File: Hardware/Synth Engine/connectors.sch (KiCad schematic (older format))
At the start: 5 parts

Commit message: connect control board to main synth schem pages
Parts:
- removed J? (x4): Conn_01x12, symbol Conn_01x12
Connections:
- net labels added: freq_fb_1, freq_fb_2, freq_fb_3, freq_fb_4
- wire segments 97 -> 105
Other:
- moved on the sheet: J?

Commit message: remove extraneous net labels
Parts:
- removed J?: Conn_01x02, symbol Conn_01x02
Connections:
- net labels removed: LFO_freq_in, LFO_freq_out
- wire segments 105 -> 101
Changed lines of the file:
@@
 Text Label 1600 6250 0    60   ~ 0
 freq_out_4
-Text Label 8000 5750 2    60   ~ 0
-LFO_freq_in
-Text Label 8000 5850 2    60   ~ 0
-LFO_freq_out
 $Comp
 L +5V #PWR?
@@
 Wire Wire Line
 	1550 2050 1600 2050
-$Comp
-L Conn_01x02 J?
-U 1 1 5C5CD696
-P 4250 5000
-F 0 "J?" H 4250 5100 50  0000 C CNN
-F 1 "Conn_01x02" H 4250 4800 50  0000 C CNN
-F 2 "" H 4250 5000 50  0001 C CNN
-F 3 "" H 4250 5000 50  0001 C CNN
-	1    4250 5000
-	-1   0    0    -1
-$EndComp
-Wire Wire Line
-	4450 5000 4600 5000
-Wire Wire Line
-	4600 5100 4450 5100
 Wire Wire Line
 	1400 2450 1600 2450
@@
 Wire Wire Line
 	8000 5350 8300 5350
-Text HLabel 8300 5750 2    60   Input ~ 0
-LFO_freq_in
-Text HLabel 8300 5850 2    60   Output ~ 0
-LFO_freq_out
-Wire Wire Line
-	8300 5750 8000 5750
-Wire Wire Line
-	8000 5850 8300 5850
-Text Label 4600 5000 0    60   ~ 0
-LFO_freq_in
-Text Label 4600 5100 0    60   ~ 0
-LFO_freq_out
 Text Label 1600 1300 0    60   ~ 0
 freq_fb_1

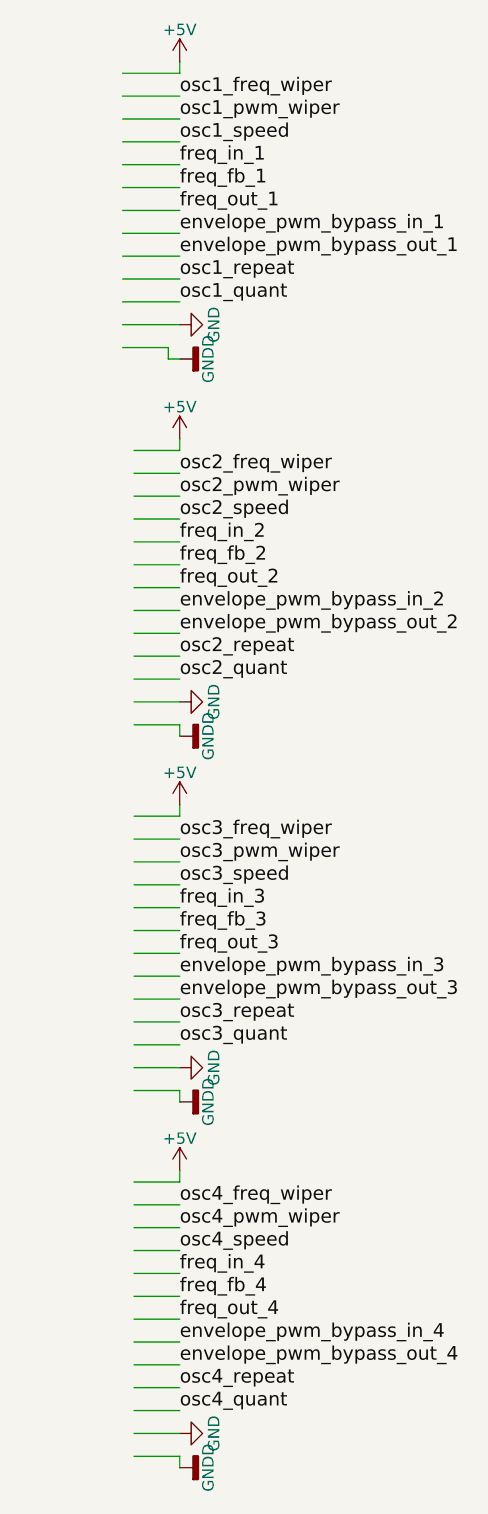
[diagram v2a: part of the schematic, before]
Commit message: fix missing connectors in main synth project
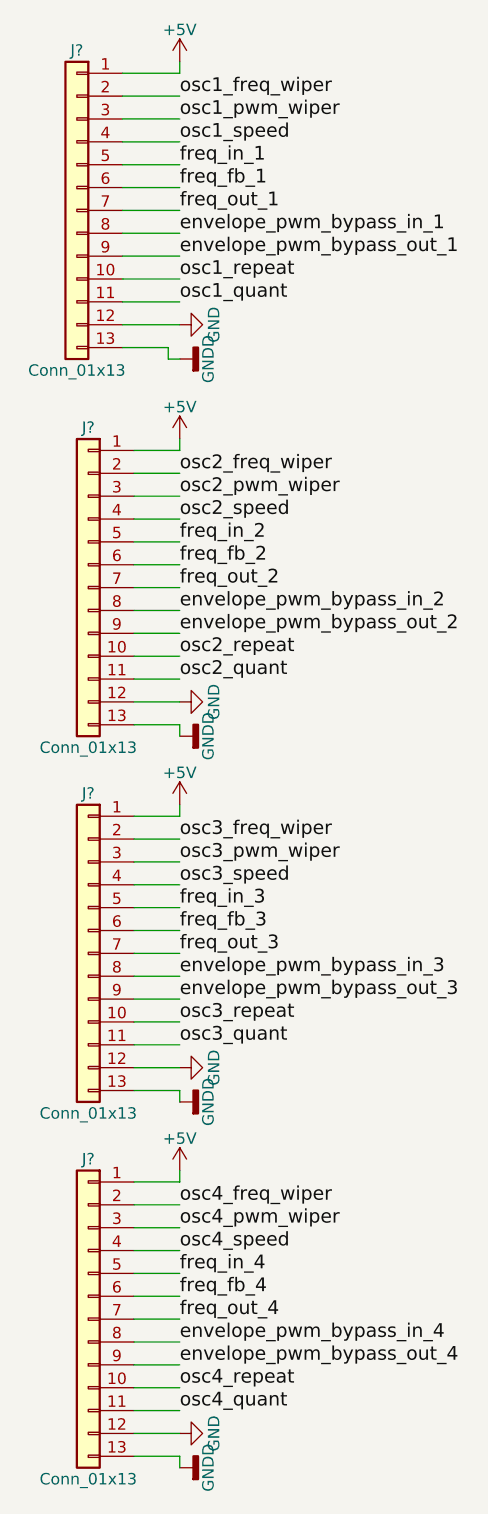
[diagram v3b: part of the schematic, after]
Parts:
- added J? (x4): Conn_01x13, symbol Conn_01x13
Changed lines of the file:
@@
 Wire Wire Line
 	8300 4850 8000 4850
+$Comp
+L Conn_01x13 J?
+U 1 1 5C5E7989
+P 1150 1400
+F 0 "J?" H 1150 2100 50  0000 C CNN
+F 1 "Conn_01x13" H 1150 700 50  0000 C CNN
+F 2 "" H 1150 1400 50  0001 C CNN
+F 3 "" H 1150 1400 50  0001 C CNN
+	1    1150 1400
+	-1   0    0    -1
+$EndComp
+$Comp
+L Conn_01x13 J?
+U 1 1 5C5E7A2D
+P 1200 3050
+F 0 "J?" H 1200 3750 50  0000 C CNN
+F 1 "Conn_01x13" H 1200 2350 50  0000 C CNN
+F 2 "" H 1200 3050 50  0001 C CNN
+F 3 "" H 1200 3050 50  0001 C CNN
+	1    1200 3050
+	-1   0    0    -1
+$EndComp
+$Comp
+L Conn_01x13 J?
+U 1 1 5C5E7A85
+P 1200 4650
+F 0 "J?" H 1200 5350 50  0000 C CNN
+F 1 "Conn_01x13" H 1200 3950 50  0000 C CNN
+F 2 "" H 1200 4650 50  0001 C CNN
+F 3 "" H 1200 4650 50  0001 C CNN
+	1    1200 4650
+	-1   0    0    -1
+$EndComp
+$Comp
+L Conn_01x13 J?
+U 1 1 5C5E7AE0
+P 1200 6250
+F 0 "J?" H 1200 6950 50  0000 C CNN
+F 1 "Conn_01x13" H 1200 5550 50  0000 C CNN
+F 2 "" H 1200 6250 50  0001 C CNN
+F 3 "" H 1200 6250 50  0001 C CNN
+	1    1200 6250
+	-1   0    0    -1
+$EndComp
 $EndSCHEMATC

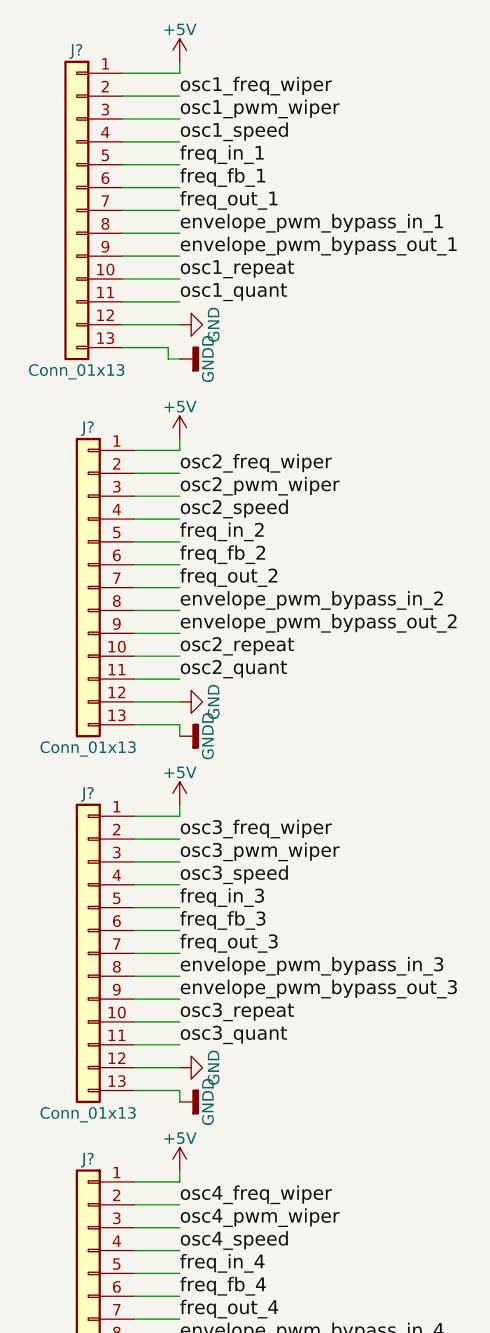
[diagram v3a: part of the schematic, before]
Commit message: remove external pull-up resistors on digital input pins. These are unecessary due to internal pull-up resistors.
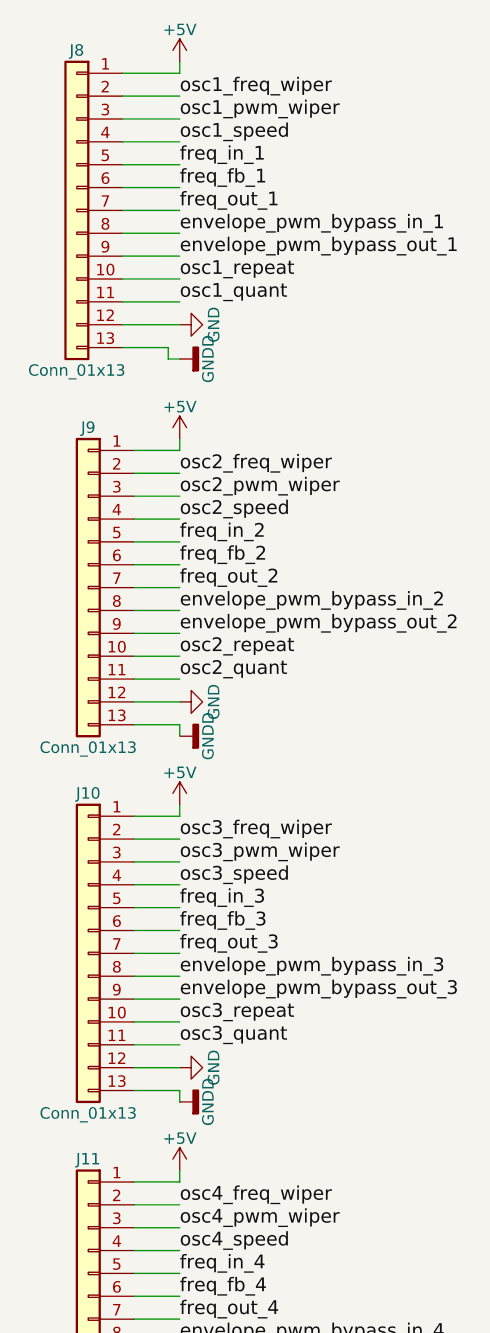
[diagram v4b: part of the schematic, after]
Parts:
- J10, J11, J8, J9: renamed from J?; footprint (none) -> Pin_Headers:Pin_Header_Straight_1x13_Pitch2.54mm
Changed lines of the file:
@@
 freq_out_4
 $Comp
-L +5V #PWR?
+L +5V #PWR0136
 U 1 1 5C5CBE8C
 P 1600 750
-F 0 "#PWR?" H 1600 600 50  0001 C CNN
+F 0 "#PWR0136" H 1600 600 50  0001 C CNN
 F 1 "+5V" H 1600 890 50  0000 C CNN
 F 2 "" H 1600 750 50  0001 C CNN
@@
 $EndComp
 $Comp
-L +5V #PWR?
+L +5V #PWR0137
 U 1 1 5C5CBFC0
 P 1600 2400
-F 0 "#PWR?" H 1600 2250 50  0001 C CNN
+F 0 "#PWR0137" H 1600 2250 50  0001 C CNN
 F 1 "+5V" H 1600 2540 50  0000 C CNN
 F 2 "" H 1600 2400 50  0001 C CNN
@@
 $EndComp
 $Comp
-L +5V #PWR?
+L +5V #PWR0138
 U 1 1 5C5CC0B3
 P 1600 4000
-F 0 "#PWR?" H 1600 3850 50  0001 C CNN
+F 0 "#PWR0138" H 1600 3850 50  0001 C CNN
 F 1 "+5V" H 1600 4140 50  0000 C CNN
 F 2 "" H 1600 4000 50  0001 C CNN
@@
 $EndComp
 $Comp
-L +5V #PWR?
+L +5V #PWR0139
 U 1 1 5C5CC16C
 P 1600 5600
-F 0 "#PWR?" H 1600 5450 50  0001 C CNN
+F 0 "#PWR0139" H 1600 5450 50  0001 C CNN
 F 1 "+5V" H 1600 5740 50  0000 C CNN
 F 2 "" H 1600 5600 50  0001 C CNN
@@
 $EndComp
 $Comp
-L GND #PWR?
+L GND #PWR0140
 U 1 1 5C5CC347
 P 1600 1900
-F 0 "#PWR?" H 1600 1650 50  0001 C CNN
+F 0 "#PWR0140" H 1600 1650 50  0001 C CNN
 F 1 "GND" H 1600 1750 50  0000 C CNN
 F 2 "" H 1600 1900 50  0001 C CNN
@@
 $EndComp
 $Comp
-L GNDD #PWR?
+L GNDD #PWR0141
 U 1 1 5C5CC457
 P 1600 2050
-F 0 "#PWR?" H 1600 1800 50  0001 C CNN
+F 0 "#PWR0141" H 1600 1800 50  0001 C CNN
 F 1 "GNDD" H 1600 1925 50  0000 C CNN
 F 2 "" H 1600 2050 50  0001 C CNN
@@
 $EndComp
 $Comp
-L GND #PWR?
+L GND #PWR0142
 U 1 1 5C5CC7AC
 P 1600 3550
-F 0 "#PWR?" H 1600 3300 50  0001 C CNN
+F 0 "#PWR0142" H 1600 3300 50  0001 C CNN
 F 1 "GND" H 1600 3400 50  0000 C CNN
 F 2 "" H 1600 3550 50  0001 C CNN
@@
 $EndComp
 $Comp
-L GNDD #PWR?
+L GNDD #PWR0143
 U 1 1 5C5CC80E
 P 1600 3700
-F 0 "#PWR?" H 1600 3450 50  0001 C CNN
+F 0 "#PWR0143" H 1600 3450 50  0001 C CNN
 F 1 "GNDD" H 1600 3575 50  0000 C CNN
 F 2 "" H 1600 3700 50  0001 C CNN
@@
 $EndComp
 $Comp
-L GND #PWR?
+L GND #PWR0144
 U 1 1 5C5CC9CC
 P 1600 5150
-F 0 "#PWR?" H 1600 4900 50  0001 C CNN
+F 0 "#PWR0144" H 1600 4900 50  0001 C CNN
 F 1 "GND" H 1600 5000 50  0000 C CNN
 F 2 "" H 1600 5150 50  0001 C CNN
@@
 $EndComp
 $Comp
-L GNDD #PWR?
+L GNDD #PWR0145
 U 1 1 5C5CC9D2
 P 1600 5300
-F 0 "#PWR?" H 1600 5050 50  0001 C CNN
+F 0 "#PWR0145" H 1600 5050 50  0001 C CNN
 F 1 "GNDD" H 1600 5175 50  0000 C CNN
 F 2 "" H 1600 5300 50  0001 C CNN
@@
 $EndComp
 $Comp
-L GND #PWR?
+L GND #PWR0146
 U 1 1 5C5CCA12
 P 1600 6750
-F 0 "#PWR?" H 1600 6500 50  0001 C CNN
+F 0 "#PWR0146" H 1600 6500 50  0001 C CNN
 F 1 "GND" H 1600 6600 50  0000 C CNN
 F 2 "" H 1600 6750 50  0001 C CNN
@@
 $EndComp
 $Comp
-L GNDD #PWR?
+L GNDD #PWR0147
 U 1 1 5C5CCA18
 P 1600 6900
-F 0 "#PWR?" H 1600 6650 50  0001 C CNN
+F 0 "#PWR0147" H 1600 6650 50  0001 C CNN
 F 1 "GNDD" H 1600 6775 50  0000 C CNN
 F 2 "" H 1600 6900 50  0001 C CNN
@@
 	8300 4850 8000 4850
 $Comp
-L Conn_01x13 J?
+L Conn_01x13 J8
 U 1 1 5C5E7989
 P 1150 1400
-F 0 "J?" H 1150 2100 50  0000 C CNN
+F 0 "J8" H 1150 2100 50  0000 C CNN
 F 1 "Conn_01x13" H 1150 700 50  0000 C CNN
-F 2 "" H 1150 1400 50  0001 C CNN
+F 2 "Pin_Headers:Pin_Header_Straight_1x13_Pitch2.54mm" H 1150 1400 50  0001 C CNN
 F 3 "" H 1150 1400 50  0001 C CNN
 	1    1150 1400
@@
 $EndComp
 $Comp
-L Conn_01x13 J?
+L Conn_01x13 J9
 U 1 1 5C5E7A2D
 P 1200 3050
-F 0 "J?" H 1200 3750 50  0000 C CNN
+F 0 "J9" H 1200 3750 50  0000 C CNN
 F 1 "Conn_01x13" H 1200 2350 50  0000 C CNN
-F 2 "" H 1200 3050 50  0001 C CNN
+F 2 "Pin_Headers:Pin_Header_Straight_1x13_Pitch2.54mm" H 1200 3050 50  0001 C CNN
 F 3 "" H 1200 3050 50  0001 C CNN
 	1    1200 3050
@@
 $EndComp
 $Comp
-L Conn_01x13 J?
+L Conn_01x13 J10
 U 1 1 5C5E7A85
 P 1200 4650
-F 0 "J?" H 1200 5350 50  0000 C CNN
+F 0 "J10" H 1200 5350 50  0000 C CNN
 F 1 "Conn_01x13" H 1200 3950 50  0000 C CNN
-F 2 "" H 1200 4650 50  0001 C CNN
+F 2 "Pin_Headers:Pin_Header_Straight_1x13_Pitch2.54mm" H 1200 4650 50  0001 C CNN
 F 3 "" H 1200 4650 50  0001 C CNN
 	1    1200 4650
@@
 $EndComp
 $Comp
-L Conn_01x13 J?
+L Conn_01x13 J11
 U 1 1 5C5E7AE0
 P 1200 6250
-F 0 "J?" H 1200 6950 50  0000 C CNN
+F 0 "J11" H 1200 6950 50  0000 C CNN
 F 1 "Conn_01x13" H 1200 5550 50  0000 C CNN
-F 2 "" H 1200 6250 50  0001 C CNN
+F 2 "Pin_Headers:Pin_Header_Straight_1x13_Pitch2.54mm" H 1200 6250 50  0001 C CNN
 F 3 "" H 1200 6250 50  0001 C CNN
 	1    1200 6250

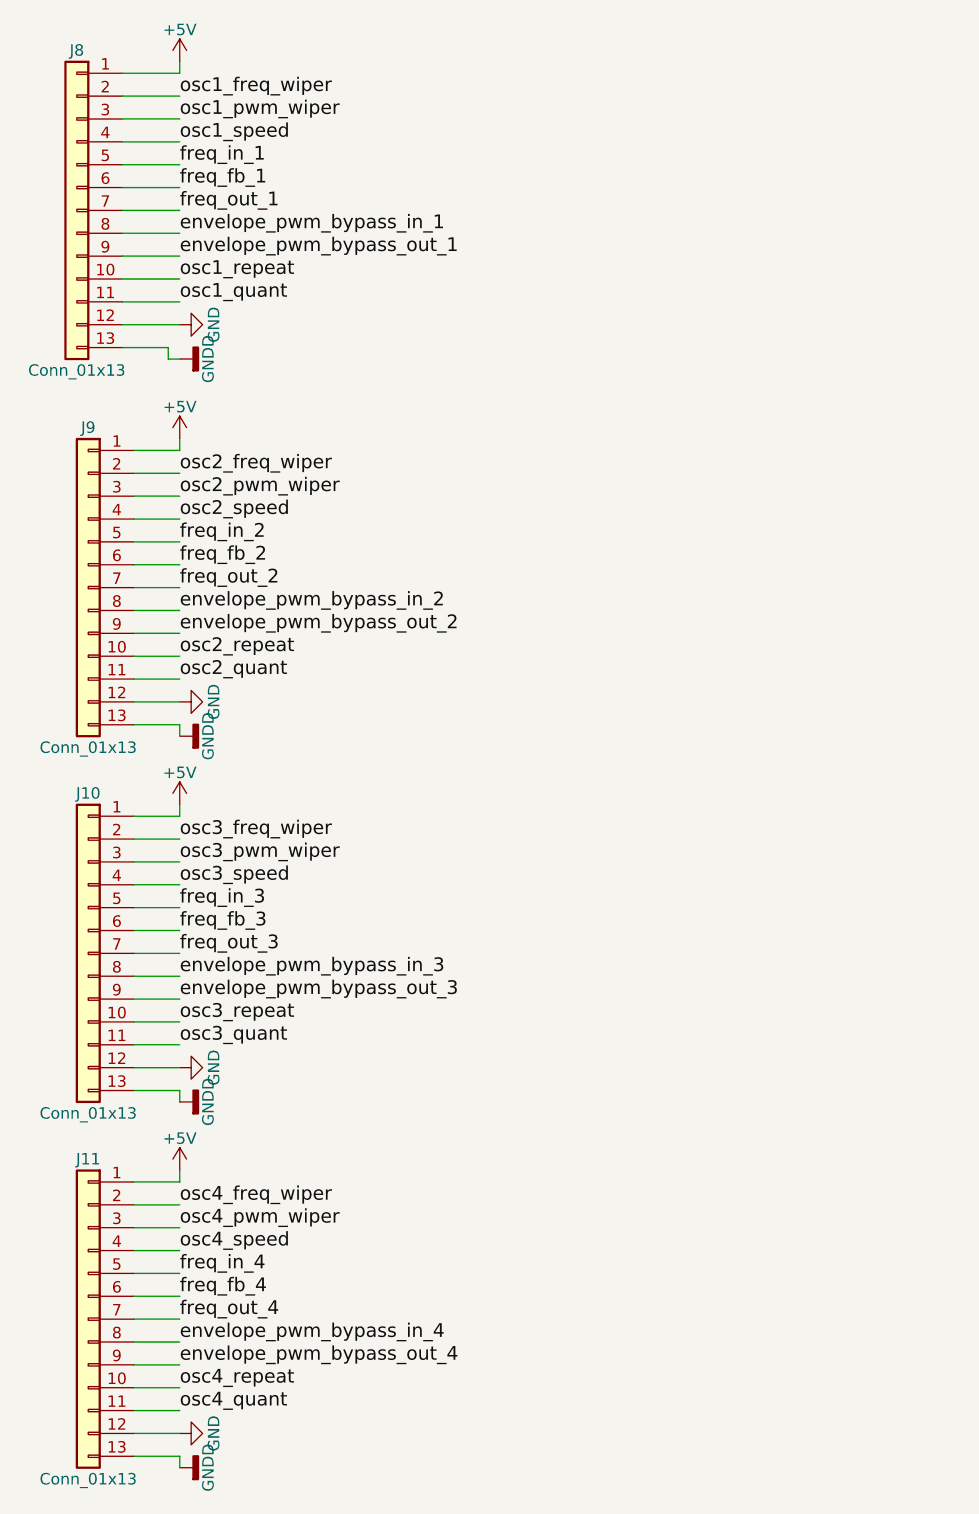
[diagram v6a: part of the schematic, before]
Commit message: match relative connector placement between two boards
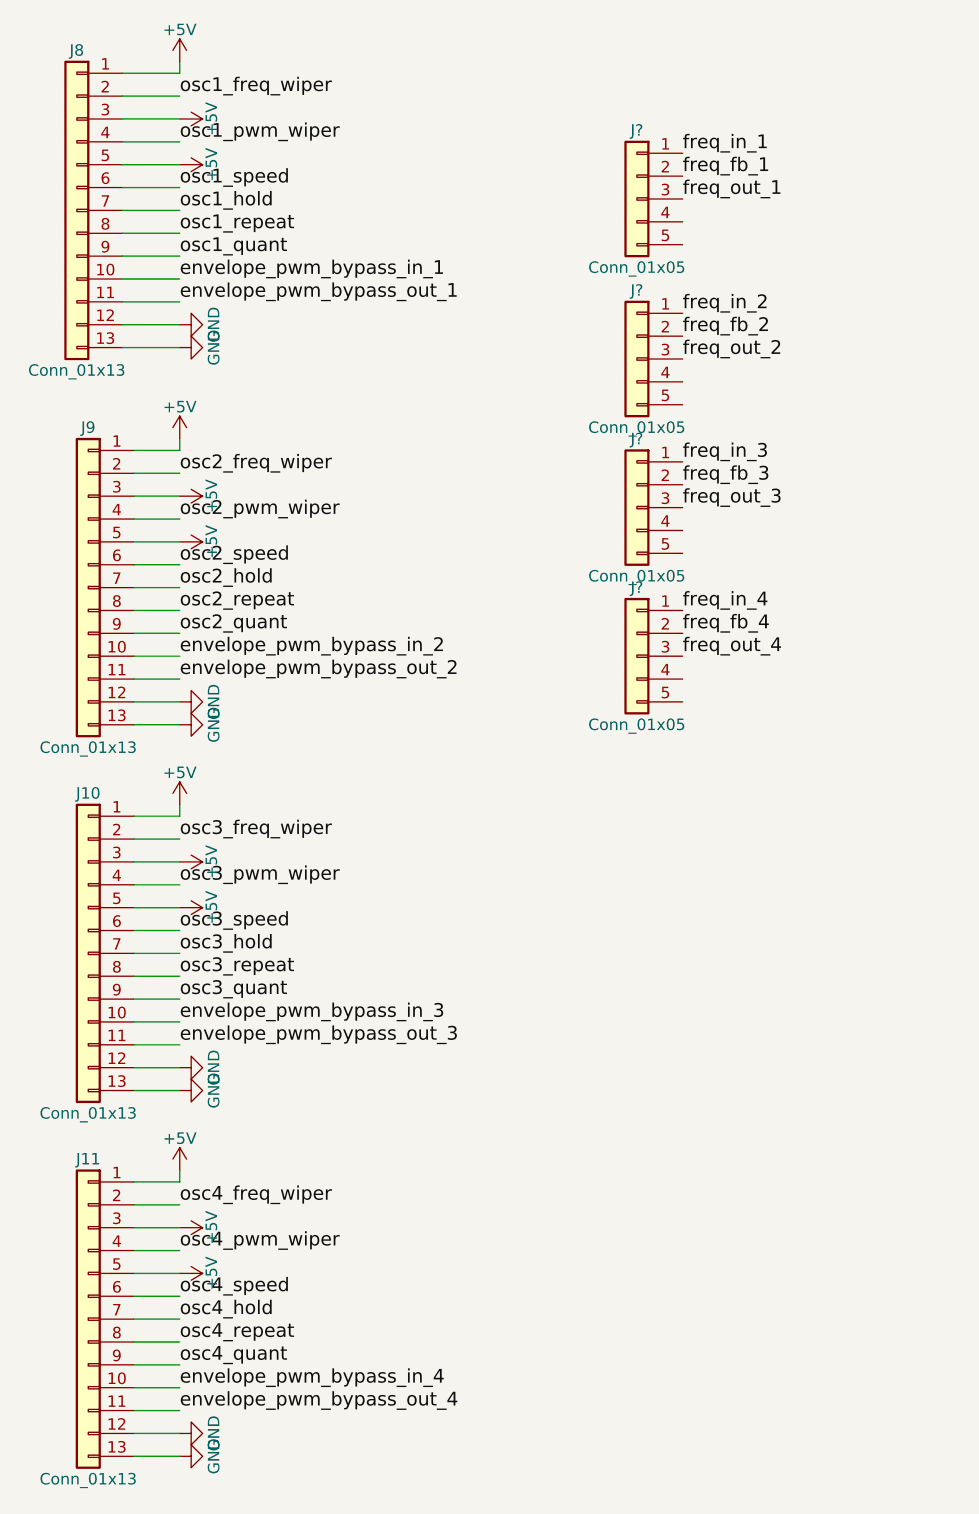
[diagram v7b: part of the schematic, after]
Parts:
- added J? (x4): Conn_01x05, symbol Conn_01x05
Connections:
- net GNDD is gone; now on net GND: J10.13 (Pin_13), J11.13 (Pin_13), J8.13 (Pin_13), J9.13 (Pin_13)
- net +5V: now also J10.3 (Pin_3), J10.5 (Pin_5), J11.3 (Pin_3), J11.5 (Pin_5), J8.3 (Pin_3), J8.5 (Pin_5), J9.3 (Pin_3), J9.5 (Pin_5)
- net envelope_pwm_bypass_in_1: now also J8.10 (Pin_10); no longer J8.8 (Pin_8)
- net envelope_pwm_bypass_in_2: now also J9.10 (Pin_10); no longer J9.8 (Pin_8)
- net envelope_pwm_bypass_in_3: now also J10.10 (Pin_10); no longer J10.8 (Pin_8)
- net envelope_pwm_bypass_in_4: now also J11.10 (Pin_10); no longer J11.8 (Pin_8)
- net envelope_pwm_bypass_out_1: now also J8.11 (Pin_11); no longer J8.9 (Pin_9)
- net envelope_pwm_bypass_out_2: now also J9.11 (Pin_11); no longer J9.9 (Pin_9)
- net envelope_pwm_bypass_out_3: now also J10.11 (Pin_11); no longer J10.9 (Pin_9)
- net envelope_pwm_bypass_out_4: now also J11.11 (Pin_11); no longer J11.9 (Pin_9)
- net freq_fb_1: now also J?.2 (Pin_2); no longer J8.6 (Pin_6)
- net freq_fb_2: now also J?.2 (Pin_2); no longer J9.6 (Pin_6)
- net freq_fb_3: now also J?.2 (Pin_2); no longer J10.6 (Pin_6)
- net freq_fb_4: now also J?.2 (Pin_2); no longer J11.6 (Pin_6)
- net freq_in_1: now also J?.1 (Pin_1); no longer J8.5 (Pin_5)
- net freq_in_2: now also J?.1 (Pin_1); no longer J9.5 (Pin_5)
- net freq_in_3: now also J?.1 (Pin_1); no longer J10.5 (Pin_5)
- net freq_in_4: now also J?.1 (Pin_1); no longer J11.5 (Pin_5)
- net freq_out_1: now also J?.3 (Pin_3); no longer J8.7 (Pin_7)
- net freq_out_2: now also J?.3 (Pin_3); no longer J9.7 (Pin_7)
- net freq_out_3: now also J?.3 (Pin_3); no longer J10.7 (Pin_7)
- net freq_out_4: now also J?.3 (Pin_3); no longer J11.7 (Pin_7)
- net osc1_pwm_wiper: now also J8.4 (Pin_4); no longer J8.3 (Pin_3)
- net osc1_quant: now also J8.9 (Pin_9); no longer J8.11 (Pin_11)
- net osc1_repeat: now also J8.8 (Pin_8); no longer J8.10 (Pin_10)
- net osc1_speed: now also J8.6 (Pin_6); no longer J8.4 (Pin_4)
- net osc2_pwm_wiper: now also J9.4 (Pin_4); no longer J9.3 (Pin_3)
- net osc2_quant: now also J9.9 (Pin_9); no longer J9.11 (Pin_11)
- net osc2_repeat: now also J9.8 (Pin_8); no longer J9.10 (Pin_10)
- net osc2_speed: now also J9.6 (Pin_6); no longer J9.4 (Pin_4)
- net osc3_pwm_wiper: now also J10.4 (Pin_4); no longer J10.3 (Pin_3)
- net osc3_quant: now also J10.9 (Pin_9); no longer J10.11 (Pin_11)
- net osc3_repeat: now also J10.8 (Pin_8); no longer J10.10 (Pin_10)
- net osc3_speed: now also J10.6 (Pin_6); no longer J10.4 (Pin_4)
- net osc4_pwm_wiper: now also J11.4 (Pin_4); no longer J11.3 (Pin_3)
- net osc4_quant: now also J11.9 (Pin_9); no longer J11.11 (Pin_11)
- net osc4_repeat: now also J11.8 (Pin_8); no longer J11.10 (Pin_10)
- net osc4_speed: now also J11.6 (Pin_6); no longer J11.4 (Pin_4)
- new net osc1_hold: J8.7 (Pin_7)
- new net osc2_hold: J9.7 (Pin_7)
- new net osc3_hold: J10.7 (Pin_7)
- new net osc4_hold: J11.7 (Pin_7)
